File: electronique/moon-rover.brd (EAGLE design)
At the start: 162.6 x 88.9 mm, 85 parts

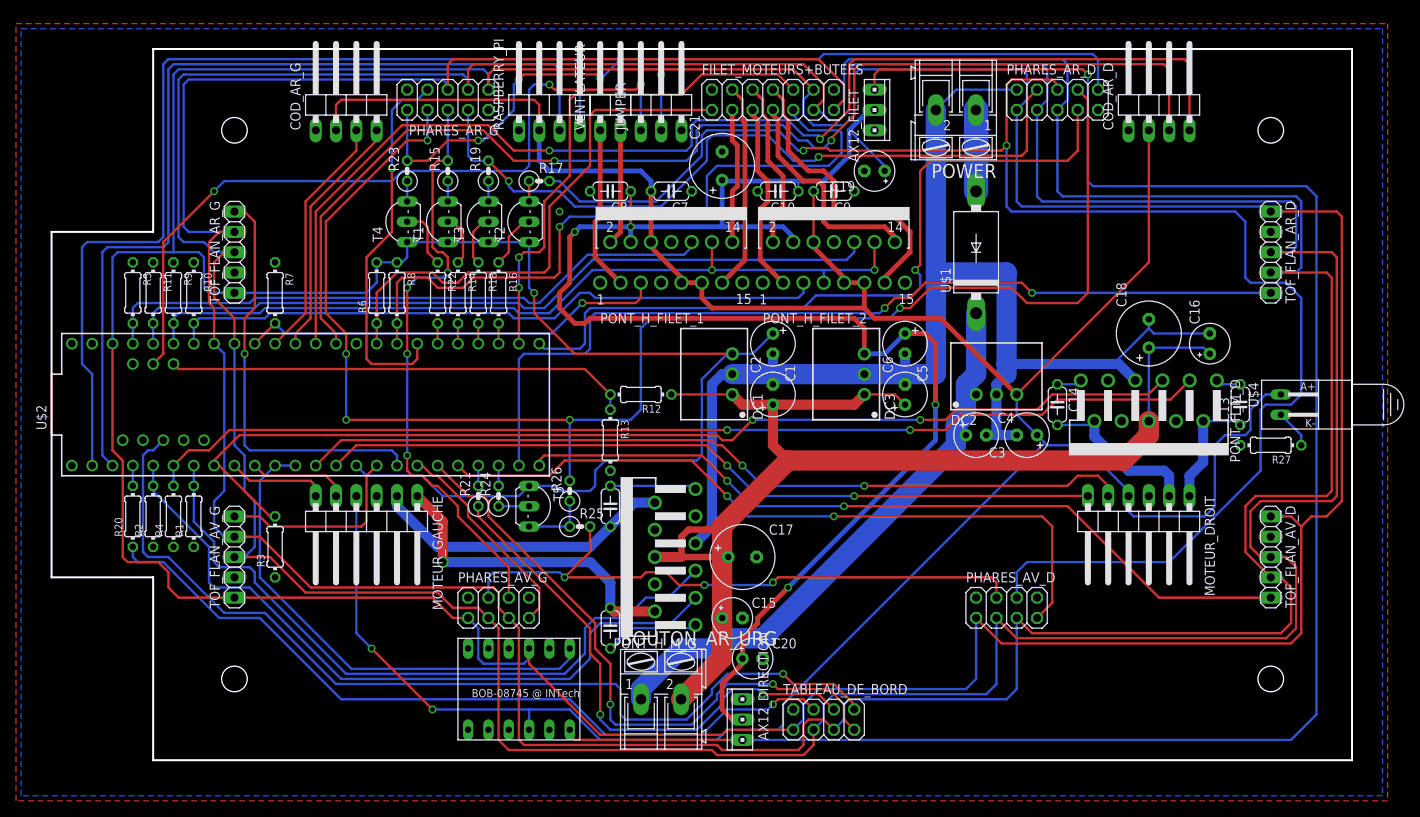
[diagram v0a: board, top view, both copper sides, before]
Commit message: maj de l'élec : réduction du coût de production
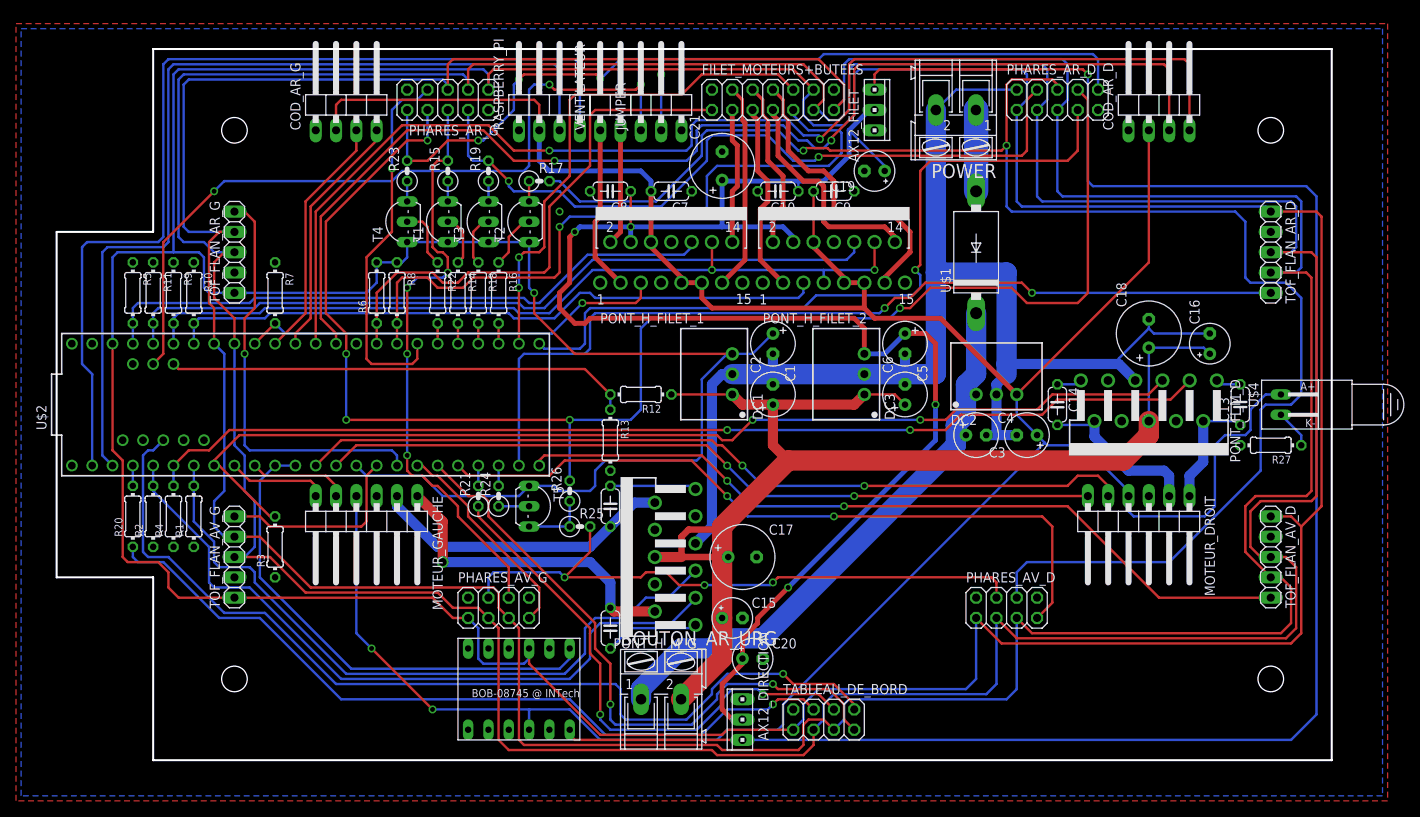
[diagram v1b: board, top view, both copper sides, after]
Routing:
- net SDA: track 490.6 -> 485.6 mm
- net SCL: track 487.9 -> 482.9 mm
- net +3V3: track 653.2 -> 648.5 mm
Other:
- board size 162.6 x 88.9 mm -> 159.4 x 88.9 mm
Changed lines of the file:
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@@
 <layer number="19" name="Unrouted" color="6" fill="1" visible="yes" active="yes"/>
 <layer number="20" name="Dimension" color="15" fill="1" visible="yes" active="yes"/>
-<layer number="21" name="tPlace" color="7" fill="1" visible="no" active="yes"/>
-<layer number="22" name="bPlace" color="7" fill="1" visible="no" active="yes"/>
-<layer number="23" name="tOrigins" color="15" fill="1" visible="no" active="yes"/>
-<layer number="24" name="bOrigins" color="15" fill="1" visible="no" active="yes"/>
-<layer number="25" name="tNames" color="7" fill="1" visible="no" active="yes"/>
-<layer number="26" name="bNames" color="7" fill="1" visible="no" active="yes"/>
+<layer number="21" name="tPlace" color="7" fill="1" visible="yes" active="yes"/>
+<layer number="22" name="bPlace" color="7" fill="1" visible="yes" active="yes"/>
+<layer number="23" name="tOrigins" color="15" fill="1" visible="yes" active="yes"/>
+<layer number="24" name="bOrigins" color="15" fill="1" visible="yes" active="yes"/>
+<layer number="25" name="tNames" color="7" fill="1" visible="yes" active="yes"/>
+<layer number="26" name="bNames" color="7" fill="1" visible="yes" active="yes"/>
 <layer number="27" name="tValues" color="7" fill="1" visible="no" active="yes"/>
 <layer number="28" name="bValues" color="7" fill="1" visible="no" active="yes"/>
@@
 <layer number="48" name="Document" color="7" fill="1" visible="yes" active="yes"/>
 <layer number="49" name="Reference" color="7" fill="1" visible="yes" active="yes"/>
-<layer number="51" name="tDocu" color="7" fill="1" visible="no" active="yes"/>
+<layer number="51" name="tDocu" color="7" fill="1" visible="yes" active="yes"/>
 <layer number="52" name="bDocu" color="7" fill="1" visible="yes" active="yes"/>
 <layer number="91" name="Nets" color="2" fill="1" visible="no" active="no"/>
@@
 <board>
 <plain>
-<wire x1="0" y1="0" x2="149.86" y2="0" width="0.254" layer="20"/>
-<wire x1="149.86" y1="0" x2="149.86" y2="88.9" width="0.254" layer="20"/>
-<wire x1="149.86" y1="88.9" x2="0" y2="88.9" width="0.254" layer="20"/>
+<wire x1="0" y1="0" x2="147.32" y2="0" width="0.254" layer="20"/>
+<wire x1="147.32" y1="0" x2="147.32" y2="88.9" width="0.254" layer="20"/>
+<wire x1="147.32" y1="88.9" x2="0" y2="88.9" width="0.254" layer="20"/>
 <wire x1="0" y1="88.9" x2="0" y2="66.04" width="0.254" layer="20"/>
 <hole x="10.16" y="10.16" drill="3.2"/>
@@
 <text x="66.04" y="96.52" size="2.54" layer="51">ARRIERE</text>
 <wire x1="0" y1="22.86" x2="0" y2="0" width="0.254" layer="20"/>
-<wire x1="-12.7" y1="22.86" x2="-12.7" y2="66.04" width="0.254" layer="20"/>
-<wire x1="0" y1="22.86" x2="-12.7" y2="22.86" width="0.254" layer="20"/>
-<wire x1="0" y1="66.04" x2="-12.7" y2="66.04" width="0.254" layer="20"/>
-<dimension x1="-12.7" y1="22.86" x2="149.86" y2="22.86" x3="68.58" y3="-25.4" layer="47"/>
-<dimension x1="149.86" y1="0" x2="149.86" y2="88.9" x3="182.88" y3="44.45" layer="47"/>
+<wire x1="-12.065" y1="22.86" x2="-12.065" y2="66.04" width="0.254" layer="20"/>
+<wire x1="0" y1="22.86" x2="-12.065" y2="22.86" width="0.254" layer="20"/>
+<wire x1="0" y1="66.04" x2="-12.065" y2="66.04" width="0.254" layer="20"/>
+<dimension x1="-12.065" y1="22.86" x2="147.32" y2="22.86" x3="67.6275" y3="-25.4" layer="47"/>
+<dimension x1="147.32" y1="0" x2="147.32" y2="88.9" x3="180.34" y3="44.45" layer="47"/>
 </plain>
 <attributes>
@@
 <wire x1="142.24" y1="14.605" x2="106.045" y2="14.605" width="0.3048" layer="1"/>
 <wire x1="106.045" y1="14.605" x2="102.87" y2="17.78" width="0.3048" layer="1"/>
-<wire x1="139.7" y1="68.58" x2="147.955" y2="68.58" width="0.3048" layer="1"/>
-<wire x1="147.955" y1="68.58" x2="148.59" y2="67.945" width="0.3048" layer="1"/>
-<wire x1="148.59" y1="67.945" x2="148.59" y2="32.385" width="0.3048" layer="1"/>
-<wire x1="148.59" y1="32.385" x2="146.685" y2="30.48" width="0.3048" layer="1"/>
-<wire x1="146.685" y1="30.48" x2="144.78" y2="30.48" width="0.3048" layer="1"/>
-<wire x1="144.78" y1="30.48" x2="143.51" y2="29.21" width="0.3048" layer="1"/>
+<wire x1="139.7" y1="68.58" x2="145.415" y2="68.58" width="0.3048" layer="1"/>
+<wire x1="145.415" y1="68.58" x2="146.05" y2="67.945" width="0.3048" layer="1"/>
+<wire x1="146.05" y1="67.945" x2="146.05" y2="31.75" width="0.3048" layer="1"/>
+<wire x1="146.05" y1="31.75" x2="143.51" y2="29.21" width="0.3048" layer="1"/>
 <wire x1="107.95" y1="81.28" x2="107.95" y2="69.85" width="0.3048" layer="16"/>
 <wire x1="107.95" y1="69.85" x2="108.585" y2="69.215" width="0.3048" layer="16"/>
@@
 <wire x1="137.16" y1="26.67" x2="137.16" y2="31.115" width="0.3048" layer="1"/>
 <wire x1="137.16" y1="31.115" x2="138.43" y2="32.385" width="0.3048" layer="1"/>
-<wire x1="138.43" y1="32.385" x2="147.32" y2="32.385" width="0.3048" layer="1"/>
-<wire x1="147.32" y1="32.385" x2="147.955" y2="33.02" width="0.3048" layer="1"/>
-<wire x1="147.955" y1="33.02" x2="147.955" y2="62.865" width="0.3048" layer="1"/>
-<wire x1="147.955" y1="62.865" x2="147.32" y2="63.5" width="0.3048" layer="1"/>
-<wire x1="147.32" y1="63.5" x2="139.7" y2="63.5" width="0.3048" layer="1"/>
+<wire x1="138.43" y1="32.385" x2="144.78" y2="32.385" width="0.3048" layer="1"/>
+<wire x1="144.78" y1="32.385" x2="145.415" y2="33.02" width="0.3048" layer="1"/>
+<wire x1="145.415" y1="33.02" x2="145.415" y2="62.865" width="0.3048" layer="1"/>
+<wire x1="145.415" y1="62.865" x2="144.78" y2="63.5" width="0.3048" layer="1"/>
+<wire x1="144.78" y1="63.5" x2="139.7" y2="63.5" width="0.3048" layer="1"/>
 <wire x1="139.7" y1="63.5" x2="142.24" y2="63.5" width="0.3048" layer="16"/>
 <wire x1="142.24" y1="63.5" x2="142.875" y2="64.135" width="0.3048" layer="16"/>
@@
 <wire x1="136.525" y1="26.035" x2="136.525" y2="31.75" width="0.3048" layer="1"/>
 <wire x1="136.525" y1="31.75" x2="137.795" y2="33.02" width="0.3048" layer="1"/>
-<wire x1="137.795" y1="33.02" x2="146.685" y2="33.02" width="0.3048" layer="1"/>
-<wire x1="146.685" y1="33.02" x2="147.32" y2="33.655" width="0.3048" layer="1"/>
-<wire x1="147.32" y1="33.655" x2="147.32" y2="60.325" width="0.3048" layer="1"/>
-<wire x1="147.32" y1="60.325" x2="146.685" y2="60.96" width="0.3048" layer="1"/>
-<wire x1="146.685" y1="60.96" x2="139.7" y2="60.96" width="0.3048" layer="1"/>
+<wire x1="137.795" y1="33.02" x2="144.145" y2="33.02" width="0.3048" layer="1"/>
+<wire x1="144.145" y1="33.02" x2="144.78" y2="33.655" width="0.3048" layer="1"/>
+<wire x1="144.78" y1="33.655" x2="144.78" y2="60.325" width="0.3048" layer="1"/>
+<wire x1="144.78" y1="60.325" x2="144.145" y2="60.96" width="0.3048" layer="1"/>
+<wire x1="144.145" y1="60.96" x2="139.7" y2="60.96" width="0.3048" layer="1"/>
 <wire x1="139.7" y1="60.96" x2="142.875" y2="60.96" width="0.3048" layer="16"/>
 <wire x1="142.875" y1="60.96" x2="143.51" y2="61.595" width="0.3048" layer="16"/>

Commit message: LL: définition des ordres décrits par la documentation, implémentation des ordres de locomotion
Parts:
- added C22, C23: (no value), 1NTech_RLCD:E2,5-6
- added DC4: R-78C9.0-1.0, dc-dc-converter:SIP3
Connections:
- new net +9V_AV: AX12_DIRECTION.2, C20.+, C22.+, DC4.3
- net +12V: now also C23.+, DC4.1
- net +9V: no longer AX12_DIRECTION.2, C20.+
- net GND: now also C22.-, C23.-, DC4.2
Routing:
- net +9V: track 197.2 -> 138.4 mm, vias 4 -> 2
- net +9V_AV: track 0.00 -> 26.3 mm
- net +12V: track 156.5 -> 173.6 mm
- net STANDBY_12V: track 74.4 -> 83.3 mm
- net +5V: track 355.5 -> 360.1 mm
- net DEL_ECLAIRAGE: track 77.7 -> 82.2 mm

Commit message: LL: debug + config + maj de l'élec
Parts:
- removed C14: 10n, 1NTech_RLCD:C050-024X044
- removed C15, C16: 1µF, 1NTech_RLCD:E2,5-5
- removed C17, C18: 220µF, 1NTech_RLCD:E3,5-8
- removed R3, R4: 10k, 1NTech_RLCD:0204/7
- added C24, C25: 100n, 1NTech_RLCD:C050-024X044
- added R28, R29: 10k, 1NTech_RLCD:0204/7
- C11, C12: value 10n -> 100n
- C13: value 10n -> (none); device 1NTech_RLCD:C050-024X044 -> resistor:E5-13
- PONT_H_M_D, PONT_H_M_G: value LM18200T -> L298; device national-semiconductor:TO-220-11 -> st-microelectronics:MULTIWATT-15
- R14, R16, R18, R22, R24: value ? -> 270
- R15, R17, R19, R20, R21, R27: value ? -> 330
- R23: value ? -> 100
- R25: value ? -> 15
- R26: value ? -> 820
- moved C12 74.1 mm to (130.8, 40.0), turned to 0 degrees
- moved C11 70.1 mm to (123.2, 40.0), turned to 0 degrees
- moved C13 62.7 mm to (76.8, 23.5), turned to 0 degrees
- moved R1 7.41 mm to (11.4, 34.3), turned to 180 degrees
- moved PONT_H_M_D 5.85 mm to (123.2, 43.8)
- moved C22 5.72 mm to (87.0, 19.7)
- moved C23 5.72 mm to (87.0, 26.0)
- moved DC4 5.72 mm to (92.1, 22.9)
- moved R2 2.54 mm to (2.54, 30.5)
- moved PONT_H_M_G 1.80 mm to (59.7, 24.1)
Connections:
- removed net MOTEUR_D_DIR: PONT_H_M_D.3, R4.2, U$2.4
- removed net MOTEUR_D_PWM: PONT_H_M_D.5, R3.2, U$2.6
- removed net MOTEUR_G_DIR: PONT_H_M_G.3, R2.2, U$2.3
- removed net MOTEUR_G_PWM: PONT_H_M_G.5, R1.2, U$2.5
- removed net N$1: C11.2, PONT_H_M_G.1
- removed net N$3: C12.1, PONT_H_M_G.11
- removed net N$6: C13.2, PONT_H_M_D.1
- removed net N$7: C14.1, PONT_H_M_D.11
- new net MOTEUR_D_A: PONT_H_M_D.12, PONT_H_M_D.5, R2.2, U$2.4
- new net MOTEUR_D_B: PONT_H_M_D.10, PONT_H_M_D.7, R1.2, U$2.6
- new net MOTEUR_G_A: PONT_H_M_G.12, PONT_H_M_G.5, R29.2, U$2.3
- new net MOTEUR_G_B: PONT_H_M_G.10, PONT_H_M_G.7, R28.2, U$2.5
- net +12V: now also C12.1, C13.+, C25.1, PONT_H_M_D.4, PONT_H_M_G.4; no longer C15.+, C16.+, C17.+, C18.+, PONT_H_M_D.6, PONT_H_M_G.6
- net +5V: now also C11.2, C24.2, PONT_H_M_D.11, PONT_H_M_D.6, PONT_H_M_D.9, PONT_H_M_G.11, PONT_H_M_G.6, PONT_H_M_G.9
- net GND: now also C11.1, C12.2, C13.-, C24.1, C25.2, PONT_H_M_D.1, PONT_H_M_D.15, PONT_H_M_D.8, PONT_H_M_G.1, PONT_H_M_G.15, PONT_H_M_G.8, R28.1, R29.1; no longer C15.-, C16.-, C17.-, C18.-, PONT_H_M_D.4, PONT_H_M_D.7, PONT_H_M_G.4, PONT_H_M_G.7, R3.1, R4.1
- net MOTEUR_D_+: now also PONT_H_M_D.14; no longer C13.1
- net MOTEUR_D_-: now also PONT_H_M_D.13, PONT_H_M_D.3; no longer C14.2, PONT_H_M_D.10
- net MOTEUR_G_+: now also PONT_H_M_G.14; no longer C11.1
- net MOTEUR_G_-: now also PONT_H_M_G.13, PONT_H_M_G.3; no longer C12.2, PONT_H_M_G.10
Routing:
- net MOTEUR_D_A: track 0.00 -> 134.5 mm, vias 0 -> 2
- net MOTEUR_D_PWM: track 134.1 -> 0.00 mm, vias 2 -> 0
- net MOTEUR_D_DIR: track 134.0 -> 0.00 mm, vias 2 -> 0
- net MOTEUR_D_B: track 0.00 -> 130.5 mm, vias 0 -> 3
- net MOTEUR_G_B: track 0.00 -> 105.3 mm, vias 0 -> 1
- net MOTEUR_G_A: track 0.00 -> 98.6 mm, vias 0 -> 1
- net +5V: track 360.1 -> 457.2 mm
- net MOTEUR_G_DIR: track 89.4 -> 0.00 mm
- net MOTEUR_G_PWM: track 87.0 -> 0.00 mm
- net MOTEUR_D_-: track 20.7 -> 44.3 mm
- net MOTEUR_G_-: track 37.9 -> 60.8 mm
- net MOTEUR_D_+: track 14.9 -> 30.9 mm
- net MOTEUR_G_+: track 40.5 -> 52.4 mm
- net N$1: track 11.9 -> 0.00 mm
- net N$3: track 10.8 -> 0.00 mm
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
